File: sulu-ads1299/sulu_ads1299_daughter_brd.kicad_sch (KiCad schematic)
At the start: 12 parts

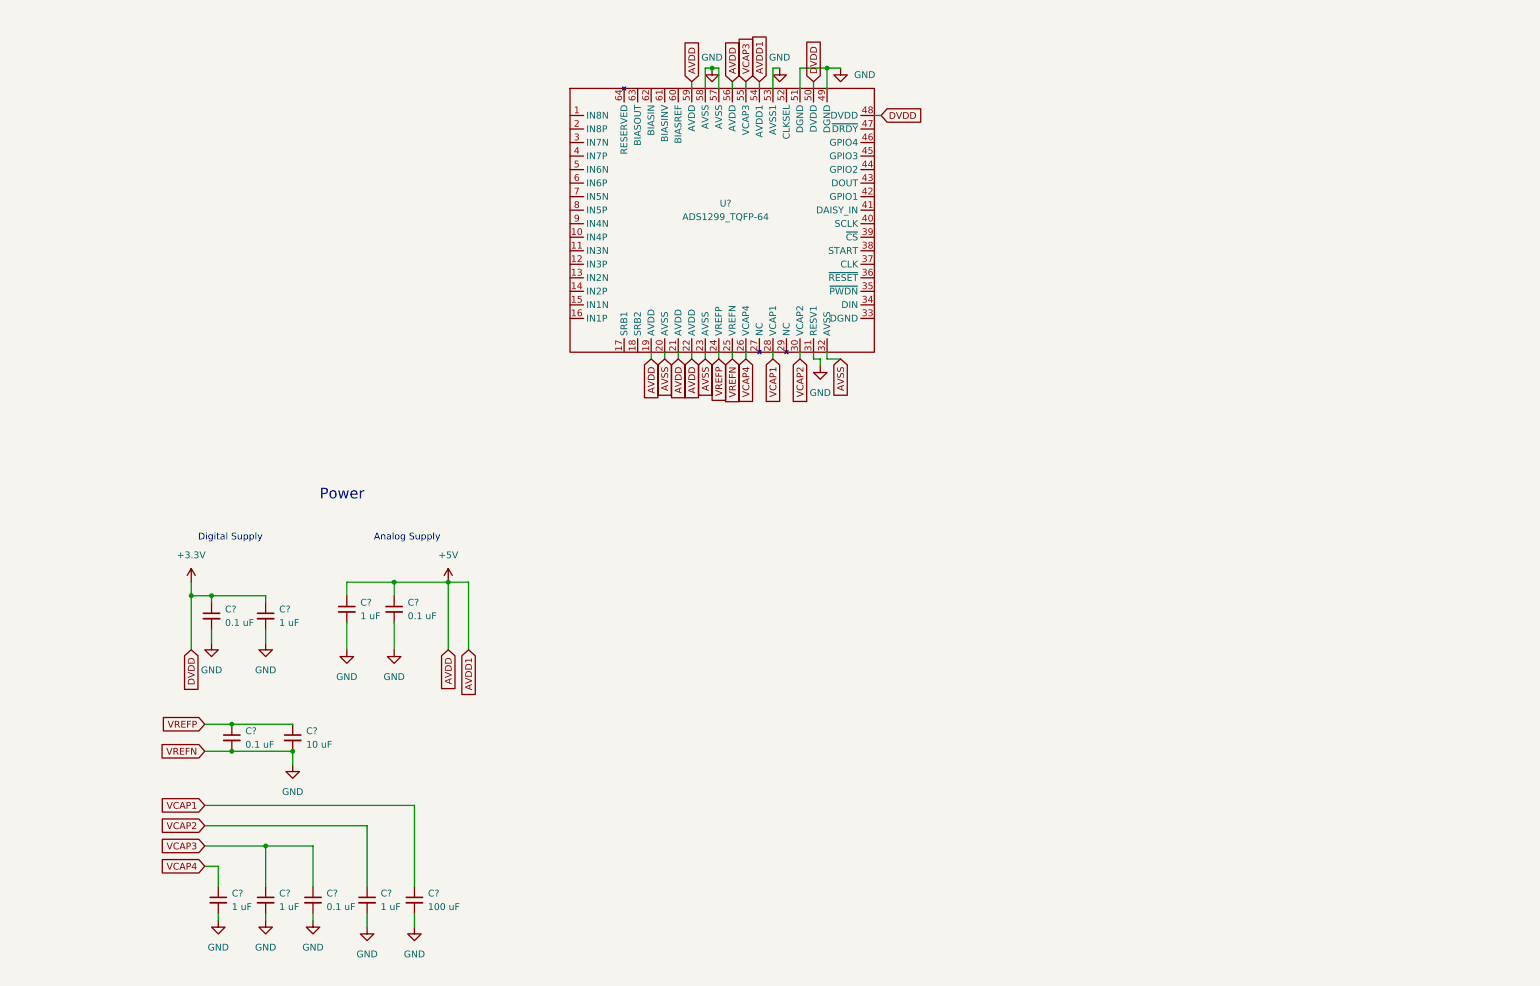
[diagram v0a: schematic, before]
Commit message: Mated connections and SPI bus
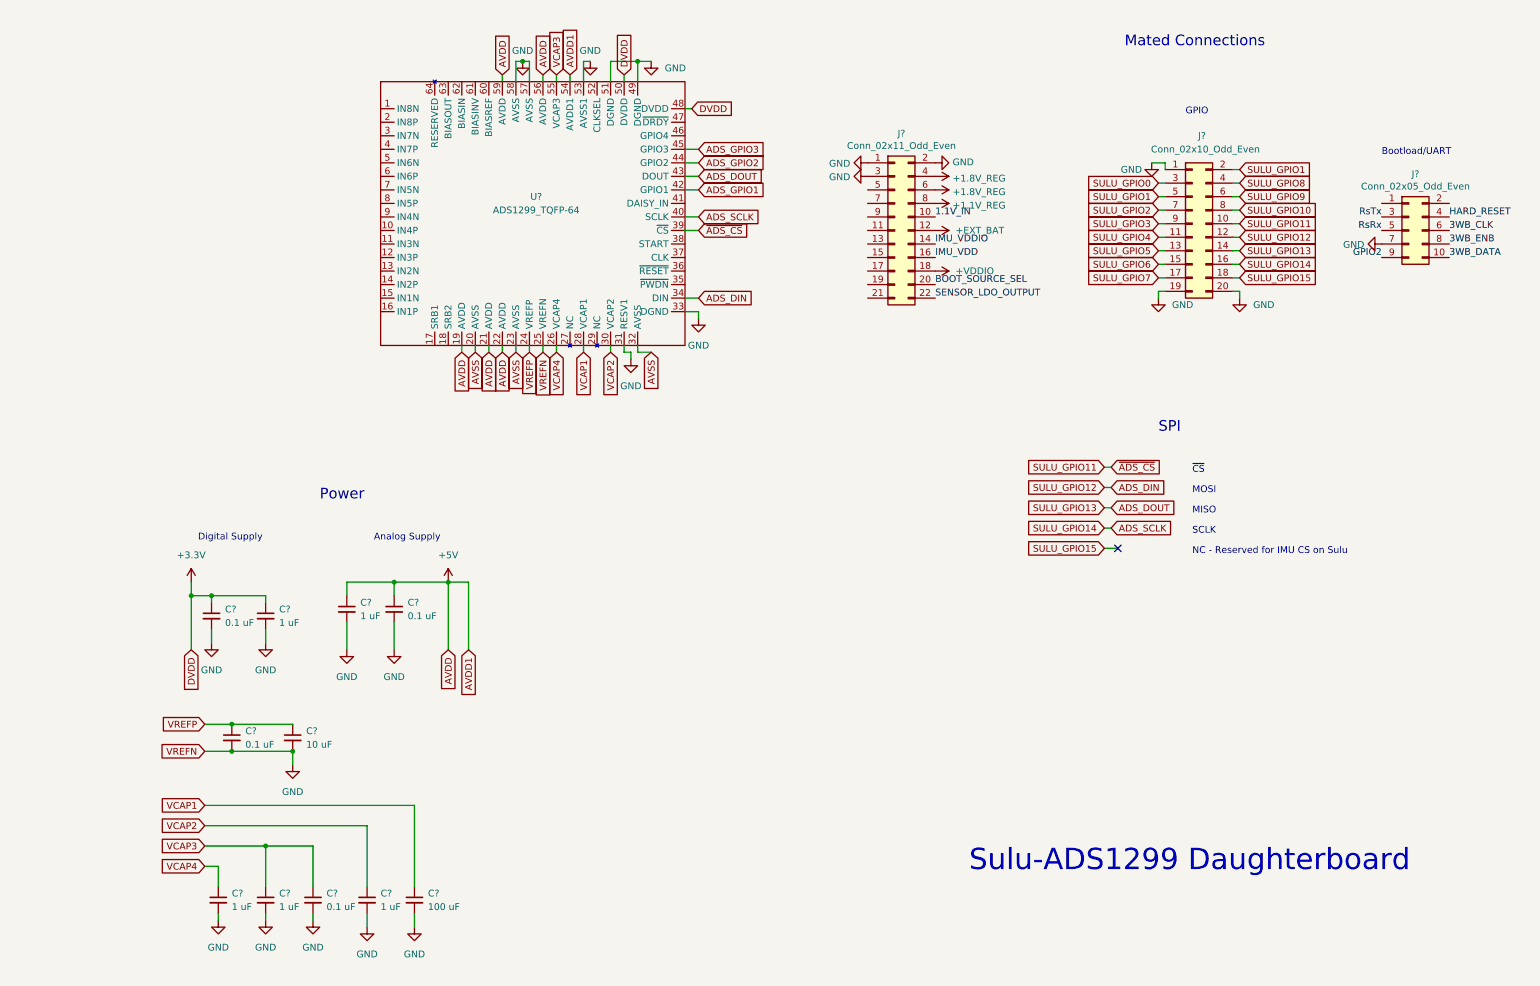
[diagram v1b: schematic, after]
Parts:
- added J?: Conn_02x10_Odd_Even, Connector_PinHeader_2.54mm:PinHeader_2x10_P2.54mm_Vertical, symbol Connector_Generic:Conn_02x10_Odd_Even
- added J?: Conn_02x05_Odd_Even, Connector_PinHeader_2.54mm:PinHeader_2x05_P2.54mm_Vertical, symbol Connector_Generic:Conn_02x05_Odd_Even
- added J?: Conn_02x11_Odd_Even, Connector_PinHeader_2.54mm:PinHeader_2x11_P2.54mm_Vertical, symbol Connector_Generic:Conn_02x11_Odd_Even
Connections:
- net GND: now also U?.33 (DGND), J?.1 (Pin_1), J?.1 (Pin_1), J?.19 (Pin_19), J?.2 (Pin_2), J?.20 (Pin_20), J?.3 (Pin_3), J?.7 (Pin_7)
- net ADS_DIN: now reaches U?.34 (DIN)
- net ADS_DIN: now also J?.12 (Pin_12)
- net SULU_GPIO11: now reaches U?.39 (~{CS})
- net SULU_GPIO11: now also J?.10 (Pin_10)
- net ADS_SCLK: now reaches U?.40 (SCLK)
- net ADS_SCLK: now also J?.16 (Pin_16)
- net ADS_GPIO1: now reaches U?.42 (GPIO1)
- net ADS_DOUT: now reaches U?.43 (DOUT)
- net ADS_DOUT: now also J?.14 (Pin_14)
- net ADS_GPIO2: now reaches U?.44 (GPIO2)
- net ADS_GPIO3: now reaches U?.45 (GPIO3)
- new net +1.1V_REG: J?.8 (Pin_8)
- new net +1.8V_REG: J?.4 (Pin_4), J?.6 (Pin_6)
- new net +EXT_BAT: J?.12 (Pin_12)
- new net +VDDIO: J?.18 (Pin_18)
- new net 1.1V_IN: J?.10 (Pin_10)
- new net 3WB_CLK: J?.6 (Pin_6)
- new net 3WB_DATA: J?.10 (Pin_10)
- new net 3WB_ENB: J?.8 (Pin_8)
- new net BOOT_SOURCE_SEL: J?.20 (Pin_20)
- new net GPIO2: J?.9 (Pin_9)
- new net HARD_RESET: J?.4 (Pin_4)
- new net IMU_VDD: J?.16 (Pin_16)
- new net IMU_VDDIO: J?.14 (Pin_14)
- new net RsRx: J?.5 (Pin_5)
- new net RsTx: J?.3 (Pin_3)
- new net SENSOR_LDO_OUTPUT: J?.22 (Pin_22)
- new net SULU_GPIO0: J?.3 (Pin_3)
- new net SULU_GPIO1: J?.2 (Pin_2), J?.5 (Pin_5)
- new net SULU_GPIO10: J?.8 (Pin_8)
- new net SULU_GPIO15: J?.18 (Pin_18)
- new net SULU_GPIO2: J?.7 (Pin_7)
- new net SULU_GPIO3: J?.9 (Pin_9)
- new net SULU_GPIO4: J?.11 (Pin_11)
- new net SULU_GPIO5: J?.13 (Pin_13)
- new net SULU_GPIO6: J?.15 (Pin_15)
- new net SULU_GPIO7: J?.17 (Pin_17)
- new net SULU_GPIO8: J?.4 (Pin_4)
- new net SULU_GPIO9: J?.6 (Pin_6)
- no-connect marks 0 -> 1
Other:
- note added: "Bootload/UART"
- note added: "GPIO"
- note added: "MISO"
- note added: "MOSI"
- note added: "Mated Connections"
- note added: "NC - Reserved for IMU CS on Sulu"
- note added: "SCLK"
- note added: "SPI"
- note added: "Sulu-ADS1299 Daughterboard"
- note added: "~{CS}"
- moved on the sheet: U?

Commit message: LDO regulator
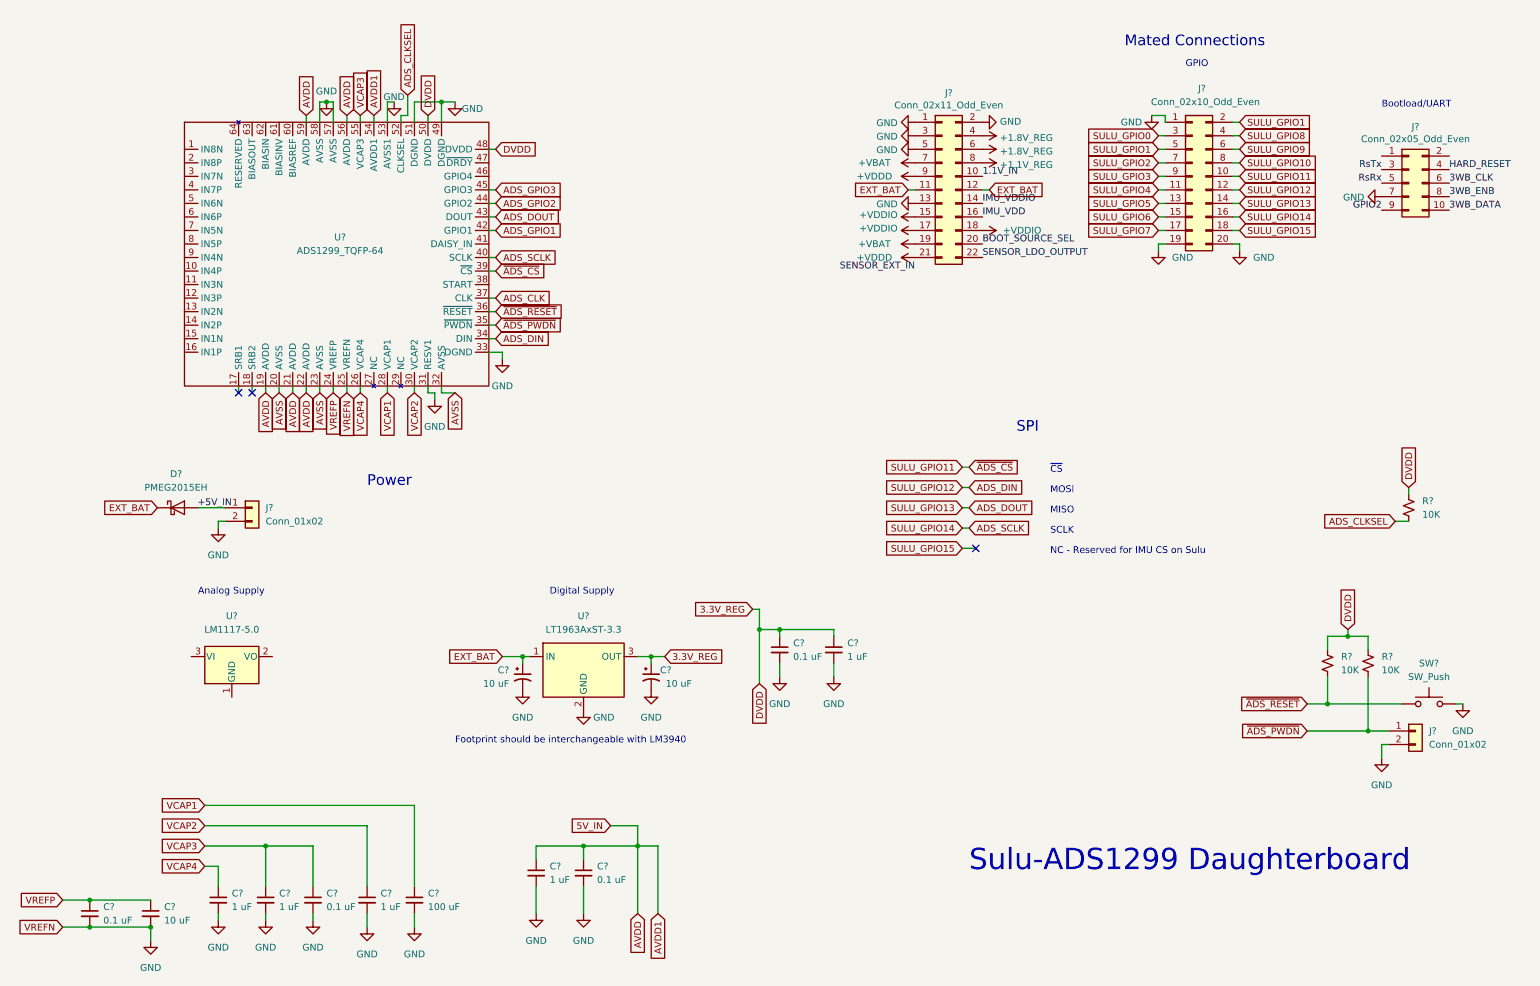
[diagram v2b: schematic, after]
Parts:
- added C? (x2): 10 uF, symbol Device:C_Polarized_Small_US
- added D?: PMEG2015EH, Diode_SMD:D_SOD-123F, symbol Diode:PMEG2015EH
- added J? (x2): Conn_01x02, symbol Connector_Generic:Conn_01x02
- added R? (x3): 10K, symbol Device:R_Small_US
- added SW?: SW_Push, symbol Switch:SW_Push
- added U?: LT1963AxST-3.3, Package_TO_SOT_SMD:SOT-223-3_TabPin2, symbol Regulator_Linear:LT1963AxST-3.3
- added U?: LM1117-5.0, symbol Regulator_Linear:LM1117-5.0
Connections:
- net +EXT_BAT is gone; now on net EXT_BAT: J?.12 (Pin_12)
- net +VDDIO: now also J?.15 (Pin_15), J?.17 (Pin_17)
- net GND: now also J?.13 (Pin_13), J?.5 (Pin_5), C?.2, C?.2, J?.2 (Pin_2), J?.2 (Pin_2), SW?.2, U?.2 (GND)
- net ~{ADS_PWDN}: now reaches U?.35 (~{PWDN})
- net ~{ADS_PWDN}: now also J?.1 (Pin_1), R?.2
- net ~{ADS_RESET}: now reaches U?.36 (~{RESET})
- net ~{ADS_RESET}: now also R?.2, SW?.1
- net ADS_CLK: now reaches U?.37 (CLK)
- net ADS_CLKSEL: now reaches U?.52 (CLKSEL)
- net ADS_CLKSEL: now also R?.2
- net EXT_BAT: now reaches J?.11 (Pin_11)
- net EXT_BAT: now also C?.1, D?.1 (K), U?.1 (IN)
- net +VBAT: now reaches J?.19 (Pin_19)
- net +VBAT: now also J?.7 (Pin_7)
- net +VDDD: now reaches J?.21 (Pin_21)
- net +VDDD: now also J?.9 (Pin_9)
- net +3.3V renamed 3.3V_REG
- net 3.3V_REG: now also C?.1, R?.1, R?.1, R?.1, U?.3 (OUT)
- net +5V renamed 5V_IN
- new net: D?.2 (A), J?.1 (Pin_1)
- no-connect marks 1 -> 3
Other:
- note added: "Footprint should be interchangeable with LM3940"
- moved on the sheet: C?, J?, U?
